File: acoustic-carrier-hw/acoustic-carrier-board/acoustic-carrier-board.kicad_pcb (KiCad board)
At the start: 6 copper layers, 78.8 x 95 mm, 361 parts, among them IC1 ECP5-BGA256, IC1101 MT41K256M16TW-107_P, J1001 BWU.FL-IPEX1, J1002 BWU.FL-IPEX1, J1003 BWU.FL-IPEX1, J1005 BWU.FL-IPEX1, J1006 BWU.FL-IPEX1, J1007 8P8C_Shielded, J1008 BWU.FL-IPEX1, J1009 BWU.FL-IPEX1, J1010 BWU.FL-IPEX1, J1201 HR911130A, J201 Conn_02x06_Odd_Even, J701 Conn_02x06_Odd_Even, J703 Conn_02x06_Odd_Even, J801 TYPE-C-31-M-12, J901 Conn_02x06_Odd_Even, Q201 AO3401A, U1001 MS9280, U1002 THS4521IDGK, U1003 DGQ2788AEN-T1-GE4, U1004 LMV321, U1005 TL432DBZ, U1201 KSZ9031RN, U201 TPS2121RUX, U202 TLV62569DBV, U203 TLV62569DBV, U204 TLV62569DBV, U205 TLV62569DBV, U206 OPA376xxDBV, U701 W25Q128JVS, U702 W25Q128JVS, U801 USB3300-EZK, U802 LMV321, Y1201 25MHz, Y401 Crystal Oscillator, Y801 Crystal_GND24_Small

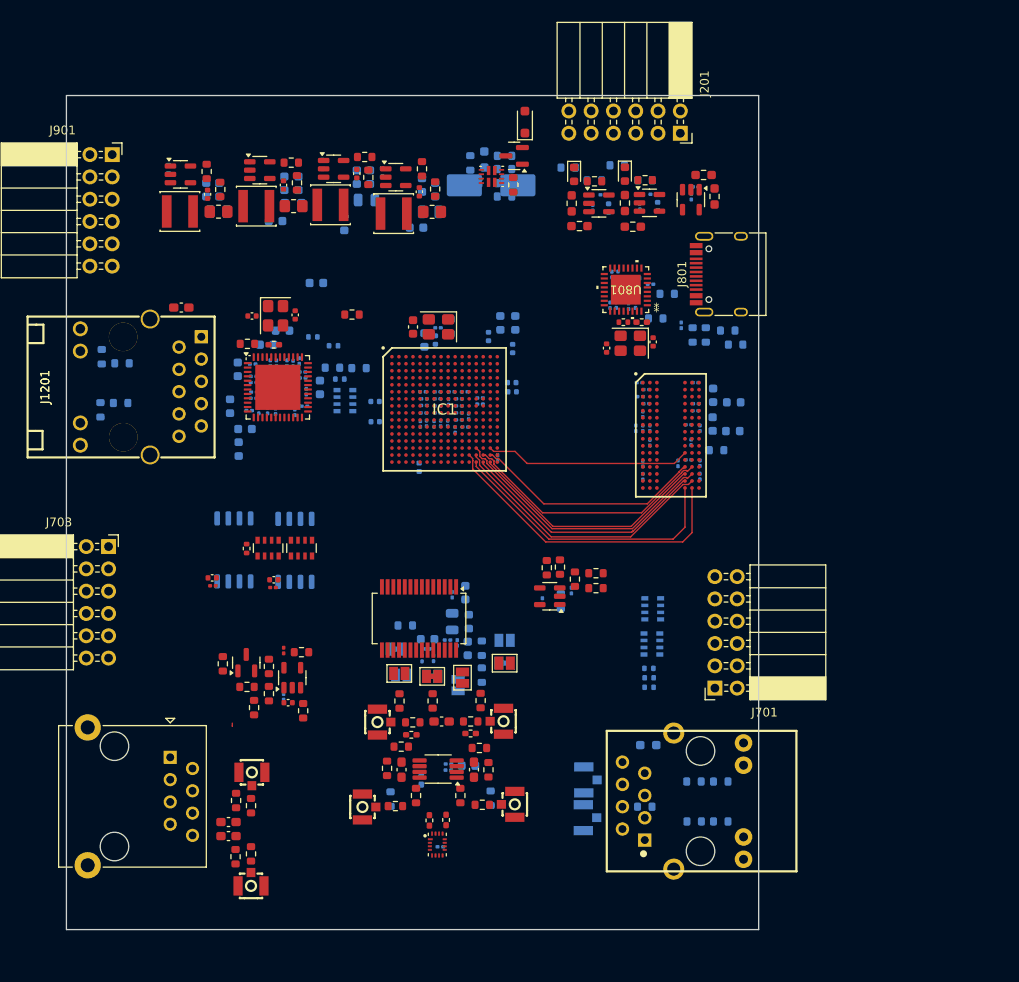
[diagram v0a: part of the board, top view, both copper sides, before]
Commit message: [carrier] Routed LDQ group and CMD-CTRL bus
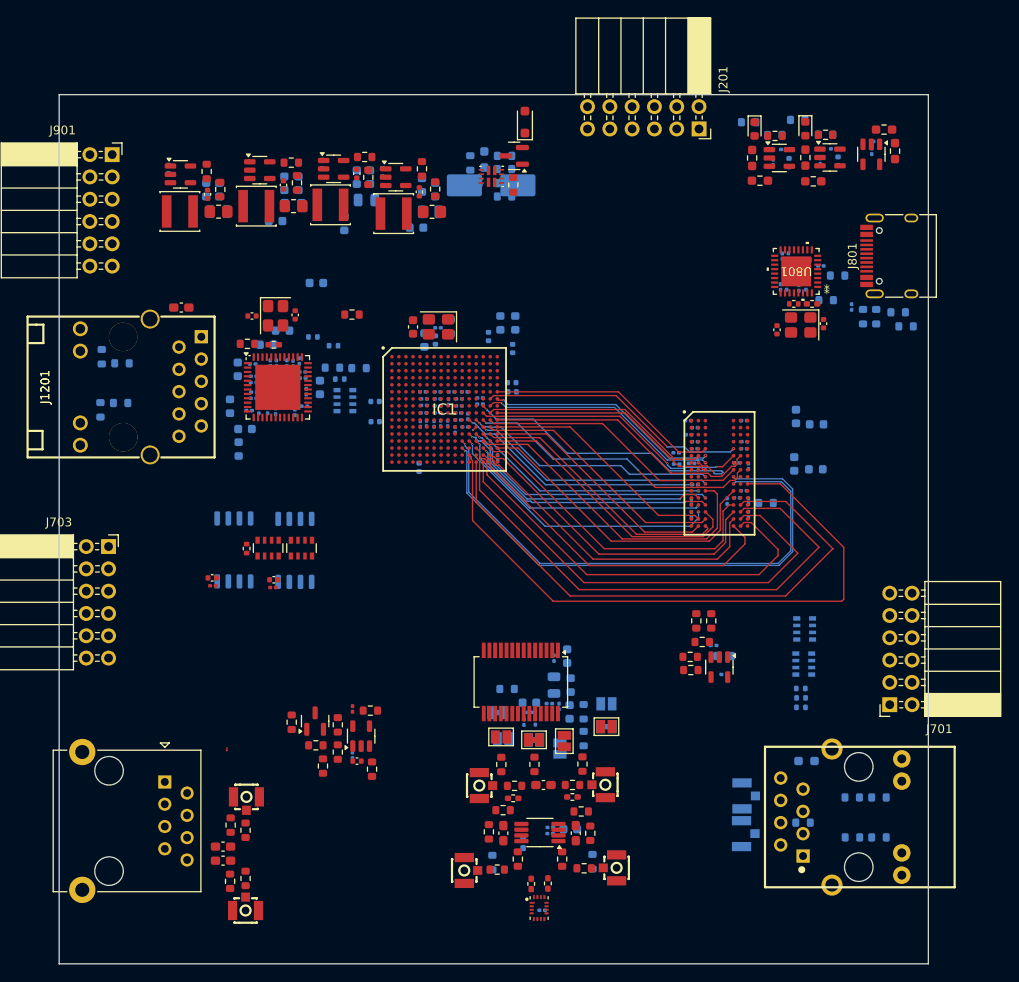
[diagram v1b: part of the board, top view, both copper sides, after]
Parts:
- moved C225 22.3 mm to (120.7, 118.0), turned to 180 degrees
- moved C801 21.2 mm to (137.6, 58.5)
- moved C802 21.2 mm to (138.1, 57.3)
- moved C805 21.2 mm to (133.7, 59.6)
- moved C808 21.2 mm to (127.5, 58.2)
- moved C822 21.2 mm to (133.2, 58.2)
- moved D802 21.2 mm to (130.0, 55.9)
- moved R802 21.2 mm to (130.9, 61.9)
- moved R803 21.2 mm to (130.0, 59.2)
- moved R811 21.2 mm to (123.9, 59.2)
- moved R813 21.2 mm to (126.5, 56.7)
- moved R814 21.2 mm to (123.5, 55.1)
- moved R816 21.2 mm to (140.2, 58.4)
- moved R818 21.2 mm to (139.0, 56.0)
- moved R826 21.2 mm to (129.1, 54.9)
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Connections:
- IC1 pad F16: /DDR3/DDR3.LDM -> /DDR3/DDR3.DQ0
- IC1 pad G15: /DDR3/DDR3.DQ7 -> /DDR3/DDR3.LDM
- IC1 pad J14: /DDR3/DDR3.DQ5 -> /DDR3/DDR3.DQ1
- IC1 pad J16: /DDR3/DDR3.DQ3 -> /DDR3/DDR3.DQ4
- IC1 pad K12: unconnected-(IC1E-PR29B-PadK12) -> /DDR3/DDR3.ODT
- IC1 pad K13: unconnected-(IC1E-PR29A/GR_PCLK3_0-PadK13) -> /DDR3/DDR3.RAS#
- IC1 pad K14: /DDR3/DDR3.DQ4 -> /DDR3/DDR3.DQ5
- IC1 pad K15: /DDR3/DDR3.DQ0 -> /DDR3/DDR3.DQ7
- IC1 pad K16: /DDR3/DDR3.DQ1 -> /DDR3/DDR3.DQ3
- IC1 pad L14: /DDR3/DDR3.A7 -> /DDR3/DDR3.CAS#
- IC1 pad L15: /DDR3/DDR3.A13 -> /DDR3/DDR3.A9
- IC1 pad L16: unconnected-(IC1E-PR26A/PCLKT3_1/RDQ32-PadL16) -> /DDR3/DDR3.A7
- IC1 pad M11: /DDR3/DDR3.RAS# -> unconnected-(IC1E-PR47A-PadM11)
- IC1 pad M13: unconnected-(IC1E-PR35C-PadM13) -> /DDR3/DDR3.BA2
- IC1 pad M14: unconnected-(IC1E-PR32D-PadM14) -> /DDR3/DDR3.CS#
- IC1 pad M15: unconnected-(IC1E-PR26D/PCLKC3_0-PadM15) -> /DDR3/DDR3.A13
- IC1 pad M16: unconnected-(IC1E-PR26C/PCLKT3_0-PadM16) -> /DDR3/DDR3.RESET#
- IC1 pad N11: /DDR3/DDR3.CK+ -> /DDR3/DDR3.CK-
- IC1 pad N12: /DDR3/DDR3.CAS# -> /DDR3/DDR3.A5
- IC1 pad N14: unconnected-(IC1E-PR35D/RDQ32-PadN14) -> /DDR3/DDR3.WE#
- IC1 pad N16: /DDR3/DDR3.A9 -> /DDR3/DDR3.A2
- IC1 pad P11: /DDR3/DDR3.CK- -> /DDR3/DDR3.CK+
- IC1 pad P12: /DDR3/DDR3.CKE -> unconnected-(IC1E-PR47D/LRC_GPLL0C_IN/RDQ44-PadP12)
- IC1 pad P13: /DDR3/DDR3.A4 -> /DDR3/DDR3.A8
- IC1 pad P14: /DDR3/DDR3.A2 -> /DDR3/DDR3.A0
- IC1 pad P15: /DDR3/DDR3.A10 -> /DDR3/DDR3.A12
- IC1 pad P16: /DDR3/DDR3.A5 -> /DDR3/DDR3.A10
- IC1 pad R12: /DDR3/DDR3.A8 -> /DDR3/DDR3.CKE
- IC1 pad R13: /DDR3/DDR3.A6 -> /DDR3/DDR3.A4
- IC1 pad R14: /DDR3/DDR3.BA1 -> /DDR3/DDR3.A11
- IC1 pad R15: /DDR3/DDR3.A12 -> /DDR3/DDR3.A1
- IC1 pad T13: /DDR3/DDR3.A14 -> /DDR3/DDR3.BA1
- IC1 pad T14: /DDR3/DDR3.A11 -> /DDR3/DDR3.A6
- IC1 pad T15: /DDR3/DDR3.A1 -> /DDR3/DDR3.A14
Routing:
- net /DDR3/DDR3.CKE: track 0.00 -> 73.7 mm
- net /DDR3/DDR3.CK+: track 0.00 -> 61.1 mm, vias 0 -> 2
- net /DDR3/DDR3.CK-: track 0.00 -> 60.6 mm, vias 0 -> 2
- net /DDR3/DDR3.WE#: track 0.00 -> 37.2 mm
- net /DDR3/DDR3.BA1: track 29.0 -> 64.8 mm
- net /DDR3/DDR3.DQ6: track 0.00 -> 33.8 mm, vias 0 -> 2
- net /DDR3/DDR3.DQ5: track 0.00 -> 33.7 mm, vias 0 -> 2
- net /DDR3/DDR3.A5: track 0.00 -> 31.9 mm, vias 0 -> 2
- net /DDR3/DDR3.DQ1: track 0.00 -> 31.8 mm, vias 0 -> 2
- net /DDR3/DDR3.DQ3: track 0.07 -> 31.7 mm
- net /DDR3/DDR3.A2: track 0.00 -> 31.6 mm
- net /DDR3/DDR3.DQ7: track 0.00 -> 31.1 mm
- net /DDR3/DDR3.LDM: track 0.00 -> 30.8 mm, vias 0 -> 2
- net /DDR3/DDR3.BA0: track 0.00 -> 30.5 mm, vias 0 -> 2
- net /DDR3/DDR3.A13: track 0.00 -> 30.2 mm
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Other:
- board size 78.8 x 95 mm -> 99 x 99 mm

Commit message: [carrier] Connected part of DQU
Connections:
- IC1 pad C15: /DDR3/DDR3.DQ10 -> /DDR3/DDR3.UDM
- IC1 pad D14: /DDR3/DDR3.DQ8 -> unconnected-(IC1D-PR2D-PadD14)
- IC1 pad E16: /DDR3/DDR3.UDM -> /DDR3/DDR3.DQ10
- IC1 pad F14: unconnected-(IC1D-PR5D-PadF14) -> /DDR3/DDR3.DQ8
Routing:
- net /DDR3/DDR3.DQ8: track 0.00 -> 31.5 mm
- net /DDR3/DDR3.DQ10: track 0.00 -> 30.4 mm

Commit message: [carrier] Routed LPDDR3 without length matching
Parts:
- moved C1125 6.84 mm to (123.5, 90.4), turned to 90 degrees
- moved C1123 0.07 mm to (116.7, 89.1)
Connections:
- IC1 pad B15: /DDR3/DDR3.DQ9 -> /DDR3/DDR3.DQ14
- IC1 pad B16: /DDR3/DDR3.DQ11 -> /DDR3/DDR3.DQ12
- IC1 pad C14: /DDR3/DDR3.DQ12 -> /DDR3/DDR3.DQ14
- IC1 pad C15: /DDR3/DDR3.UDM -> /DDR3/DDR3.DQ15
- IC1 pad C16: /DDR3/DDR3.DQ14 -> /DDR3/DDR3.DQ13
- IC1 pad D14: unconnected-(IC1D-PR2D-PadD14) -> /DDR3/DDR3.DQ9
- IC1 pad E14: /DDR3/DDR3.DQ15 -> /DDR3/DDR3.DQ11
- IC1 pad F13: unconnected-(IC1D-PR8C-PadF13) -> /DDR3/DDR3.UDM
- IC1 pad F15: /DDR3/DDR3.DQ13 -> unconnected-(IC1D-PR11C-PadF15)
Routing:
- net /DDR3/DDR3.UDQS-: track 0.01 -> 33.3 mm, vias 0 -> 2
- net /DDR3/DDR3.UDQS+: track 0.15 -> 32.7 mm, vias 0 -> 2
- net /DDR3/DDR3.DQ14: track 0.00 -> 32.3 mm, vias 0 -> 2
- net /DDR3/DDR3.DQ12: track 0.00 -> 29.6 mm
- net /DDR3/DDR3.DQ9: track 0.00 -> 29.3 mm
- net /DDR3/DDR3.UDM: track 0.00 -> 29.1 mm, vias 0 -> 2
- net /DDR3/DDR3.DQ15: track 0.00 -> 28.4 mm
- net /DDR3/DDR3.DQ11: track 0.00 -> 27.2 mm, vias 0 -> 2
- net /DDR3/DDR3.DQ13: track 0.00 -> 25.6 mm
